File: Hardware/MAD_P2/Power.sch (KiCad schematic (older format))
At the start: 71 parts, among them J1 Line_3, J2 Line_1, J3 Line_2, J4 Power_In, U10 AMS1117-3.3, U11 APM4953, U12 APM4953, U19 AMS1117-1.8, U2 XL1509-5.0, U20 LM321, U21 APM4953, U3 XL1509-5.0, U4 XL1509-5.0, U5 XL1509-5.0, U6 AMS1117-3.3, U7 AMS1117-3.3, U8 AMS1117-3.3, U9 AMS1117-3.3

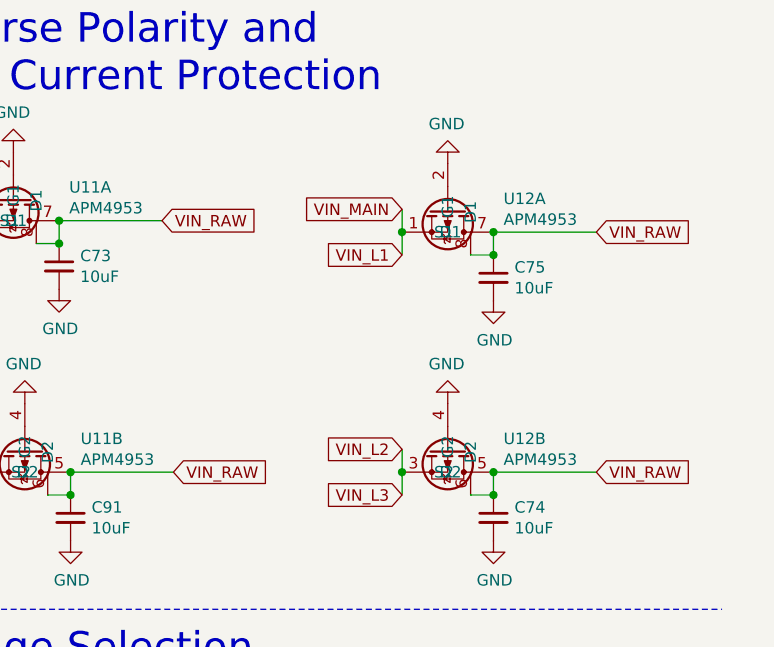
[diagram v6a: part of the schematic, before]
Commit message: replaced ads131E with ads131A
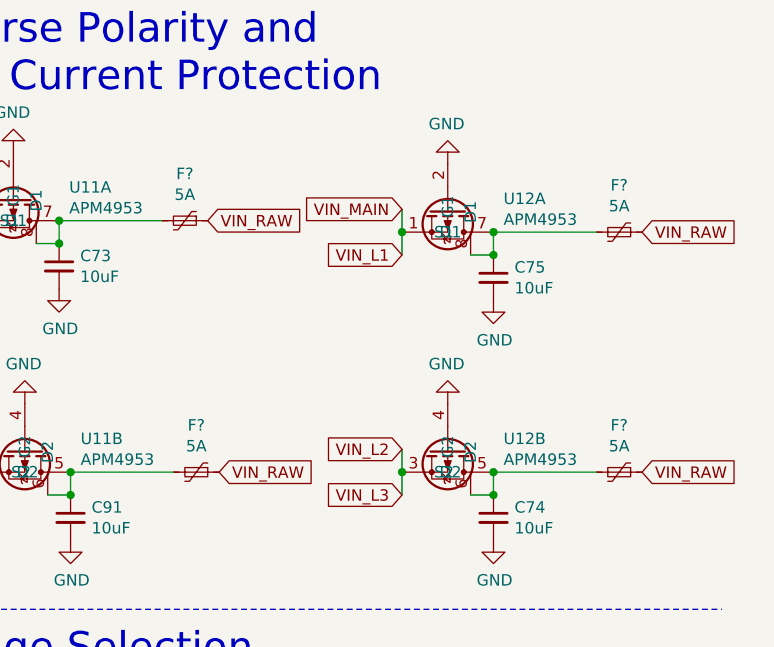
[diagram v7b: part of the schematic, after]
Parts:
- added F? (x4): 5A, symbol Device:Polyfuse_Small
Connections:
- net VIN_RAW: now also F?.1, F?.1, F?.1, F?.1; no longer C73.1, C74.1, C75.1, C91.1, U11.5 (D2), U11.6 (D2), U11.7 (D1), U11.8 (D1), U12.5 (D2), U12.6 (D2), U12.7 (D1), U12.8 (D1)
- new net: C91.1, F?.2, U11.5 (D2), U11.6 (D2)
- new net: C73.1, F?.2, U11.7 (D1), U11.8 (D1)
- new net: C74.1, F?.2, U12.5 (D2), U12.6 (D2)
- new net: C75.1, F?.2, U12.7 (D1), U12.8 (D1)
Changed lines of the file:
@@
 	1    0    0    -1
 $EndComp
-Text GLabel 10650 2800 2    50   Input ~ 0
+Text GLabel 10850 2800 2    50   Input ~ 0
 VIN_RAW
 Wire Wire Line
@@
 Text GLabel 9800 3750 0    50   Input ~ 0
 VIN_L2
-Text GLabel 8750 2750 2    50   Input ~ 0
+Text GLabel 8950 2750 2    50   Input ~ 0
 VIN_RAW
 Wire Wire Line
@@
 $EndComp
 Connection ~ 10200 3850
-Text GLabel 10650 3850 2    50   Input ~ 0
+Text GLabel 10850 3850 2    50   Input ~ 0
 VIN_RAW
 $Comp
@@
 Text GLabel 7950 3850 0    50   Input ~ 0
 VIN_ADC
-Text GLabel 8800 3850 2    50   Input ~ 0
+Text GLabel 9000 3850 2    50   Input ~ 0
 VIN_RAW
 Connection ~ 8350 3850
@@
 	4900 6900 4800 6900
 Connection ~ 4800 6900
+$Comp
+L Device:Polyfuse_Small F?
+U 1 1 60B225D6
+P 8850 2750
+F 0 "F?" V 8645 2750 50  0000 C CNN
+F 1 "5A" V 8736 2750 50  0000 C CNN
+F 2 "" H 8900 2550 50  0001 L CNN
+F 3 "~" H 8850 2750 50  0001 C CNN
+	1    8850 2750
+	0    1    1    0
+$EndComp
+$Comp
+L Device:Polyfuse_Small F?
+U 1 1 60B239BA
+P 8900 3850
+F 0 "F?" V 8695 3850 50  0000 C CNN
+F 1 "5A" V 8786 3850 50  0000 C CNN
+F 2 "" H 8950 3650 50  0001 L CNN
+F 3 "~" H 8900 3850 50  0001 C CNN
+	1    8900 3850
+	0    1    1    0
+$EndComp
+$Comp
+L Device:Polyfuse_Small F?
+U 1 1 60B24B24
+P 10750 3850
+F 0 "F?" V 10545 3850 50  0000 C CNN
+F 1 "5A" V 10636 3850 50  0000 C CNN
+F 2 "" H 10800 3650 50  0001 L CNN
+F 3 "~" H 10750 3850 50  0001 C CNN
+	1    10750 3850
+	0    1    1    0
+$EndComp
+$Comp
+L Device:Polyfuse_Small F?
+U 1 1 60B25972
+P 10750 2800
+F 0 "F?" V 10545 2800 50  0000 C CNN
+F 1 "5A" V 10636 2800 50  0000 C CNN
+F 2 "" H 10800 2600 50  0001 L CNN
+F 3 "~" H 10750 2800 50  0001 C CNN
+	1    10750 2800
+	0    1    1    0
+$EndComp
 $EndSCHEMATC
